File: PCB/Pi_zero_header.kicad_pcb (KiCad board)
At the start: 2 copper layers, 30 x 65 mm, 109 parts, among them J1 Raspberry_Pi_2_3, J10 Conn_01x04, J11 Conn_01x04, J12 Conn_01x04, J13 Conn_01x07, J14 Conn_01x03, J15 Conn_01x04, J16 Conn_01x04, J2 USB_C_Receptacle_USB2.0, J3 Conn_01x02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

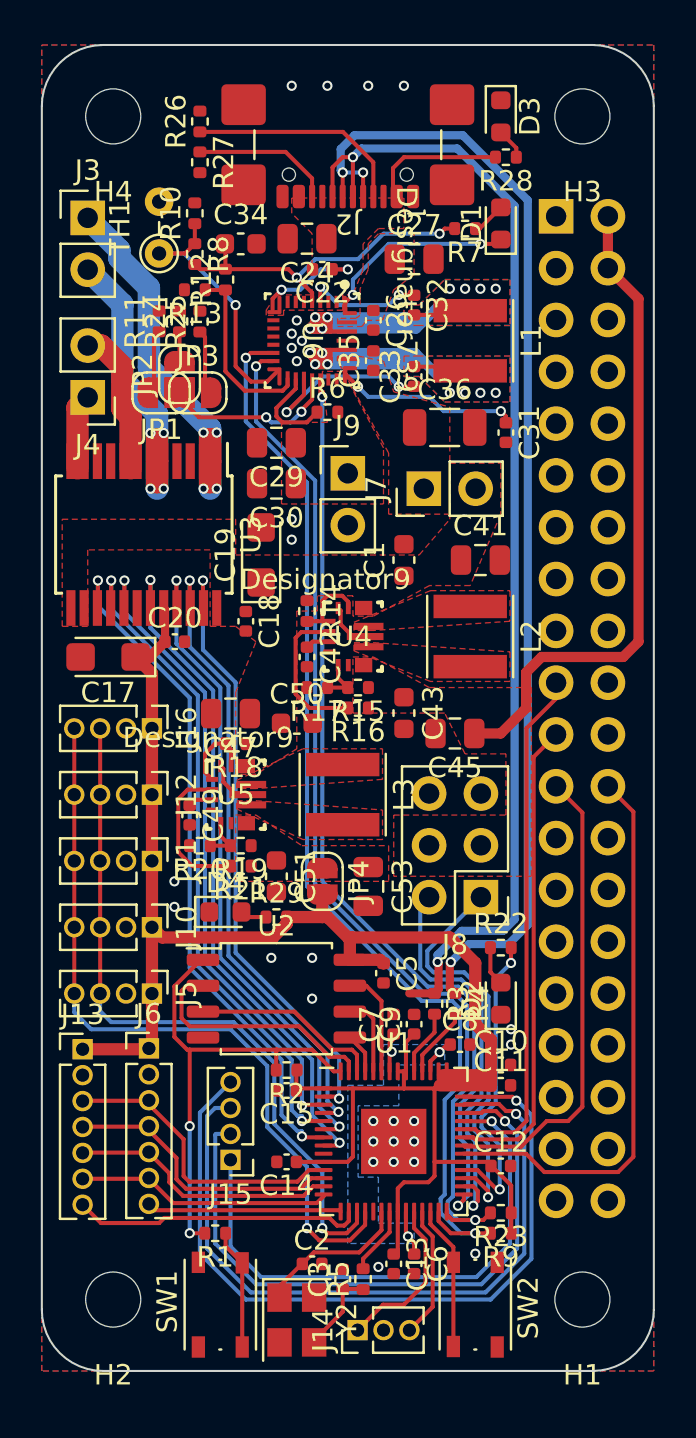
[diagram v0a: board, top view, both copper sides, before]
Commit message: Added exact components to BOM
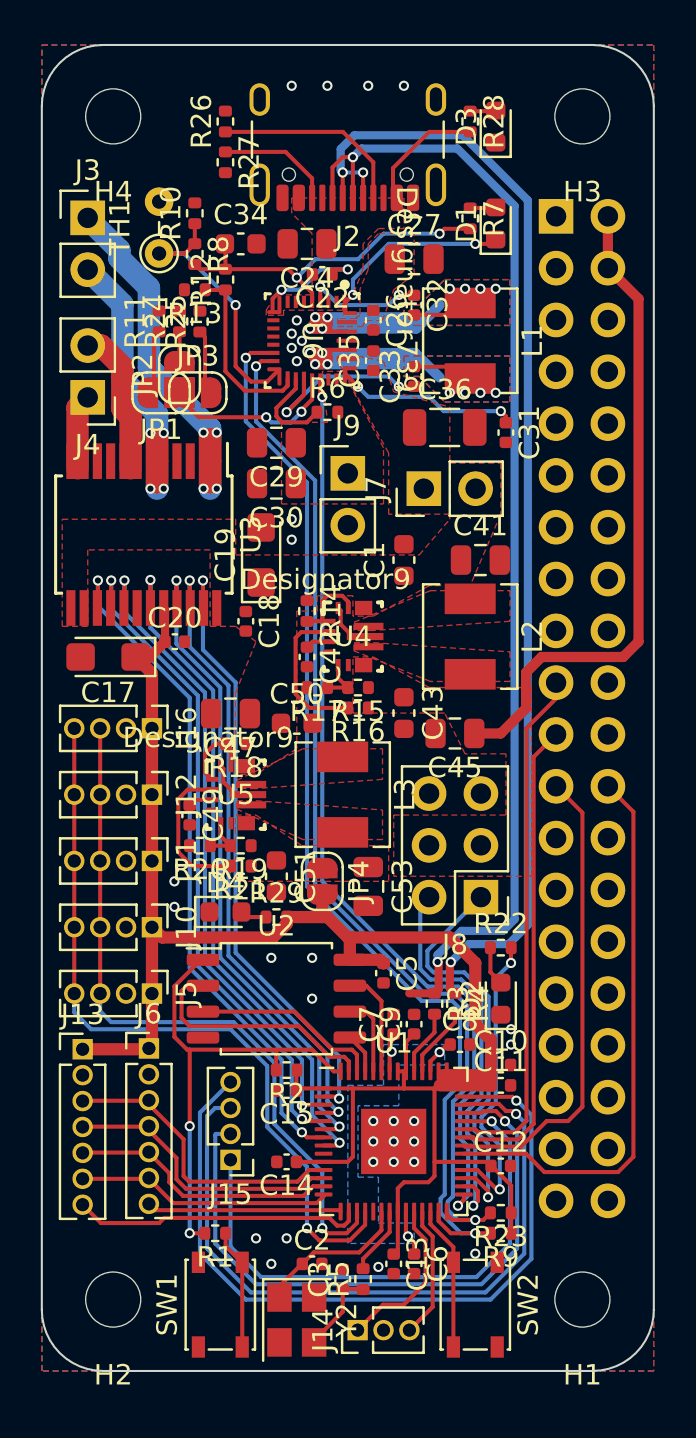
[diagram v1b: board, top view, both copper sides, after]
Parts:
- J2: footprint Connector_USB:USB_C_Receptacle_GCT_USB4110 -> Connector_USB:USB_C_Receptacle_HCTL_HC-TYPE-C-16P-01A
- L1, L2, L3: footprint Inductor_SMD:L_Vishay_IFSC-1515AH_4x4x1.8mm -> Inductor_SMD:L_Chilisin_BMRA00040420
- R10: value 30k31 -> 30k1
- R11: value 3k -> 3k01
- R8: value 5k24 -> 5k23
- SW1, SW2: footprint Button_Switch_SMD:SW_Push_1P1T_NO_Vertical_Wuerth_434133025816 -> Button_Switch_SMD:SW_SPST_PTS810
- moved R28 2.47 mm to (61.0, 56.2), turned to -90 degrees
- moved R26 1.25 mm to (49.0, 56.2)
- moved R27 1.25 mm to (49.0, 58.2)
- moved D3 0.56 mm to (62.2, 56.5), turned to 90 degrees
- moved R7 0.56 mm to (61.0, 61.0), turned to -90 degrees
- moved C22 0.25 mm to (53.8, 63.8)
- moved C24 0.25 mm to (53.0, 62.2)
- moved D1 0.25 mm to (62.2, 61.2)
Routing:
- net Net-(J2-CC2): track 6.93 -> 5.68 mm
- net Net-(J2-CC1): track 10.8 -> 9.55 mm
- net /REGN: track 16.8 -> 17.5 mm
- net VBUS: track 12.4 -> 11.7 mm
- net GND: vias 29 -> 32

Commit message: Added a LED
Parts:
- added D5: LED, LED_SMD:LED_0603_1608Metric, F.Cu at (47.8, 56.5)
- added R30: 470R, Resistor_SMD:R_0402_1005Metric, F.Cu at (48.2, 54.5)
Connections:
- net Net-(U1-GPIO21) renamed /SW_LED_1
- U1 pad 9: unconnected-(U1-GPIO7-Pad9) -> /SW_LED_2
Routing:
- net /SW_LED_2: track 0.00 -> 69.1 mm, vias 0 -> 2
- net /USB_D+: track 56.5 -> 55.3 mm
- net Net-(D5-A): track 0.00 -> 1.22 mm
- net Net-(J10-Pin_4): track 37.3 -> 36.8 mm
- net GND: vias 32 -> 39

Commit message: Ufff...
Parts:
- D3, D4: footprint LED_SMD:LED_0603_1608Metric -> LED_SMD:LED_0805_2012Metric
- moved R28 1.82 mm to (61.5, 54.5), turned to 180 degrees
- moved D3 0.25 mm to (62.2, 56.8)
- moved D4 0.25 mm to (48.8, 95.0)
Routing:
- net VBUS: track 11.7 -> 13.5 mm
- net GND: vias 39 -> 41

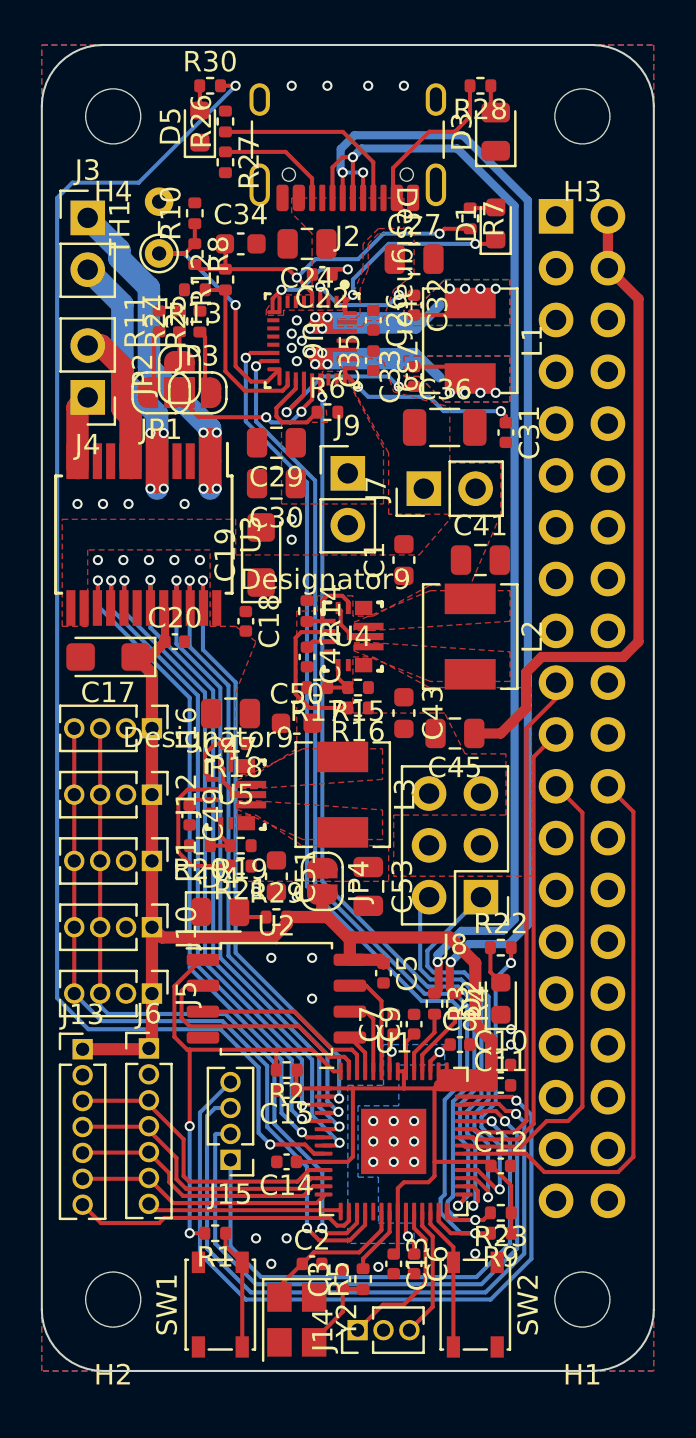
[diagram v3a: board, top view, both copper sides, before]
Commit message: Forgot about the inductors...
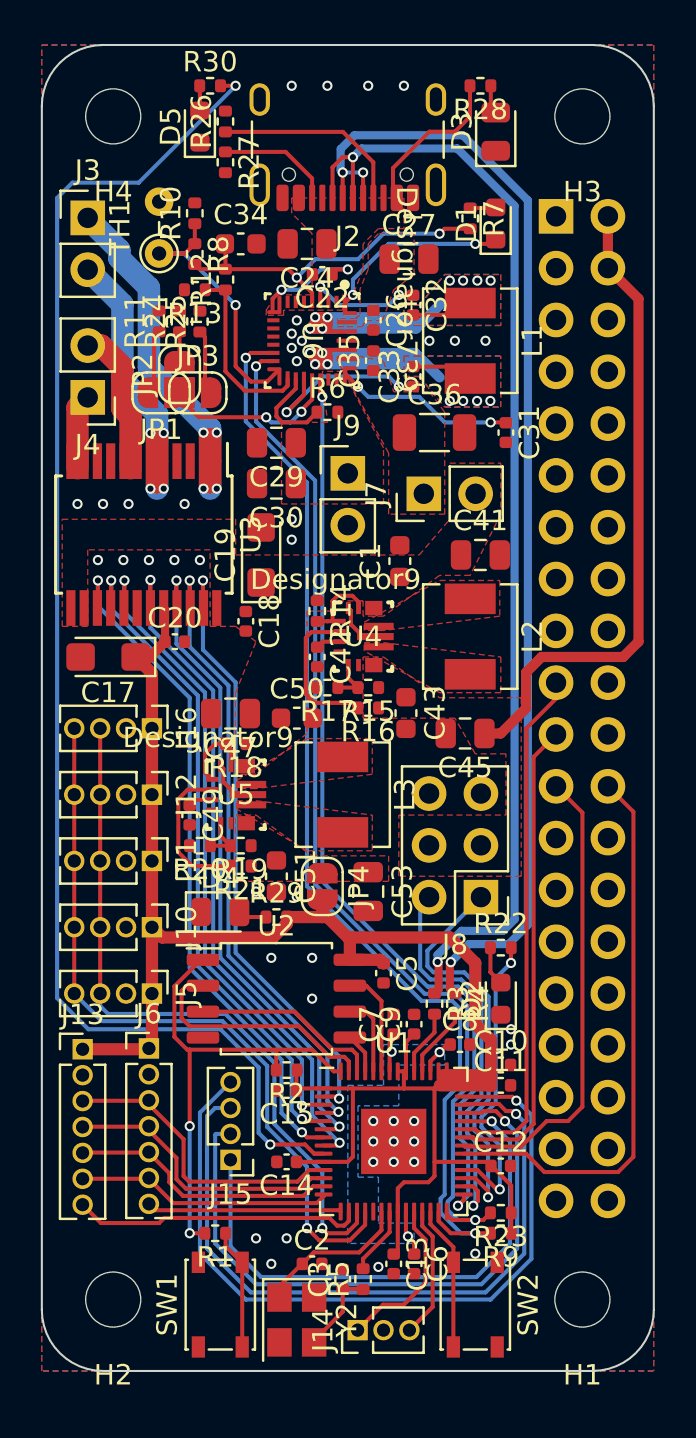
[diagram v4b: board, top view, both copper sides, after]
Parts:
- moved C36 0.56 mm to (59.2, 71.5)
- moved C42 0.50 mm to (53.5, 82.5)
- moved C45 0.50 mm to (60.8, 86.2)
- moved R14 0.50 mm to (53.5, 80.2)
- moved R15 0.50 mm to (56.0, 84.0)
- moved R16 0.50 mm to (56.0, 85.0)
- moved R17 0.50 mm to (54.0, 84.0)
- moved U4 0.50 mm to (55.8, 81.5)
- moved C27 0.25 mm to (58.0, 63.0)
- moved C41 0.25 mm to (61.5, 77.5)
- moved C50 0.25 mm to (52.5, 85.5)
- moved C53 0.25 mm to (56.0, 94.0)
- moved J7 0.25 mm to (58.7, 74.5)
- moved JP4 0.25 mm to (53.8, 93.8)
- moved C1 0.21 mm to (57.5, 77.8)
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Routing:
- net GND: vias 41 -> 44

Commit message: Hehe, logos
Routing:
- net Net-(U6-SW1): track 25.7 -> 25.9 mm, vias 8 -> 10
- net Net-(U6-SW2): track 25.7 -> 25.8 mm, vias 8 -> 10
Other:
- board text added: "+"
- board text added: "+-"
- board text added: "-"
- board text added: "-+"
- board text added: "2s 1s 3s"
- board text added: "PLAJTA corp."
- board text added: "S"
- board text added: "VOŠ a SPŠE Plzeň"
- board text added: "analog"
- board text added: "cs"

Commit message: Repaired some shish...
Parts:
- moved J6 0.25 mm to (45.2, 101.9)
- moved J13 0.21 mm to (42.0, 101.9)
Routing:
- net Net-(J2-CC2): track 5.68 -> 6.34 mm
- net Net-(J10-Pin_4): track 36.8 -> 37.3 mm
- net Net-(J10-Pin_3): track 34.9 -> 35.5 mm
- net /SW_LED_2: track 69.1 -> 69.7 mm
- net GND: vias 44 -> 73
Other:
- board text added: "EWRWC"

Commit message: Yet another mistake.
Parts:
- moved J2 1.25 mm to (55.0, 55.0)
- moved C24 1.25 mm to (53.0, 61.0)
- moved D2 1.00 mm to (62.5, 98.2)
- moved C1 0.75 mm to (57.5, 77.0)
- moved C41 0.75 mm to (61.5, 76.8)
- moved C42 0.75 mm to (53.5, 81.8)
- moved L1 0.75 mm to (61.0, 66.2)
- moved L2 0.75 mm to (61.0, 80.8)
- moved R14 0.75 mm to (53.5, 79.5)
- moved R15 0.75 mm to (56.0, 83.2)
- moved R16 0.75 mm to (56.0, 84.2)
- moved R17 0.75 mm to (54.0, 83.2)
- moved R22 0.75 mm to (62.5, 96.0)
- moved U4 0.75 mm to (55.8, 80.8)
- moved C22 0.75 mm to (53.8, 63.0)
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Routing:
- net /SDA_PWR: track 52.0 -> 53.3 mm
- net /INT_N_PWR: track 45.8 -> 47.2 mm
- net /SCL_PWR: track 54.4 -> 55.7 mm
- net /USB_D-: track 57.0 -> 58.3 mm
- net /USB_D+: track 55.3 -> 56.5 mm
- net /SW_LED_1: track 15.0 -> 15.9 mm
- net GND: track 4.59 -> 3.71 mm, vias 73 -> 91
- net Net-(J2-CC2): track 6.34 -> 6.94 mm
- net Net-(J8-Pin_2): track 19.5 -> 20.1 mm
- net Net-(J8-Pin_1): track 20.2 -> 20.8 mm

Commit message: Added pull-ups
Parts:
- added R31: 10k, Resistor_SMD:R_0402_1005Metric, F.Cu at (51.5, 108.0)
- added R32: 10k, Resistor_SMD:R_0402_1005Metric, F.Cu at (51.5, 109.0)
- moved R1 0.75 mm to (47.8, 110.8)
- moved C14 0.35 mm to (51.8, 107.0)
- moved J15 0.25 mm to (49.0, 107.2)
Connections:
- U1 pad 11: Net-(J13-Pin_3) -> Net-(J10-Pin_3)
- U1 pad 12: Net-(J13-Pin_4) -> Net-(J10-Pin_4)
- U1 pad 13: Net-(J13-Pin_5) -> Net-(J13-Pin_3)
- U1 pad 14: Net-(J13-Pin_6) -> Net-(J13-Pin_4)
- U1 pad 15: Net-(J6-Pin_7) -> Net-(J13-Pin_5)
- U1 pad 16: Net-(J13-Pin_7) -> Net-(J13-Pin_6)
- U1 pad 17: Net-(J10-Pin_3) -> Net-(J6-Pin_7)
- U1 pad 18: Net-(J10-Pin_4) -> Net-(J13-Pin_7)
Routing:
- net Net-(J10-Pin_3): track 35.5 -> 31.5 mm
- net Net-(J10-Pin_4): track 37.3 -> 33.3 mm
- net +3V3: track 94.4 -> 97.4 mm
- net Net-(J6-Pin_7): track 9.45 -> 11.7 mm
- net Net-(J13-Pin_6): track 12.5 -> 14.6 mm
- net Net-(J13-Pin_7): track 14.3 -> 16.0 mm
- net Net-(J13-Pin_5): track 12.9 -> 14.2 mm
- net Net-(J13-Pin_3): track 14.7 -> 15.5 mm
- net Net-(J13-Pin_4): track 13.8 -> 14.4 mm
- net GND: vias 91 -> 88
